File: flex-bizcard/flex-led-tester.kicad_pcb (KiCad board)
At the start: 2 copper layers, 71.8 x 34.6 mm, 4 parts

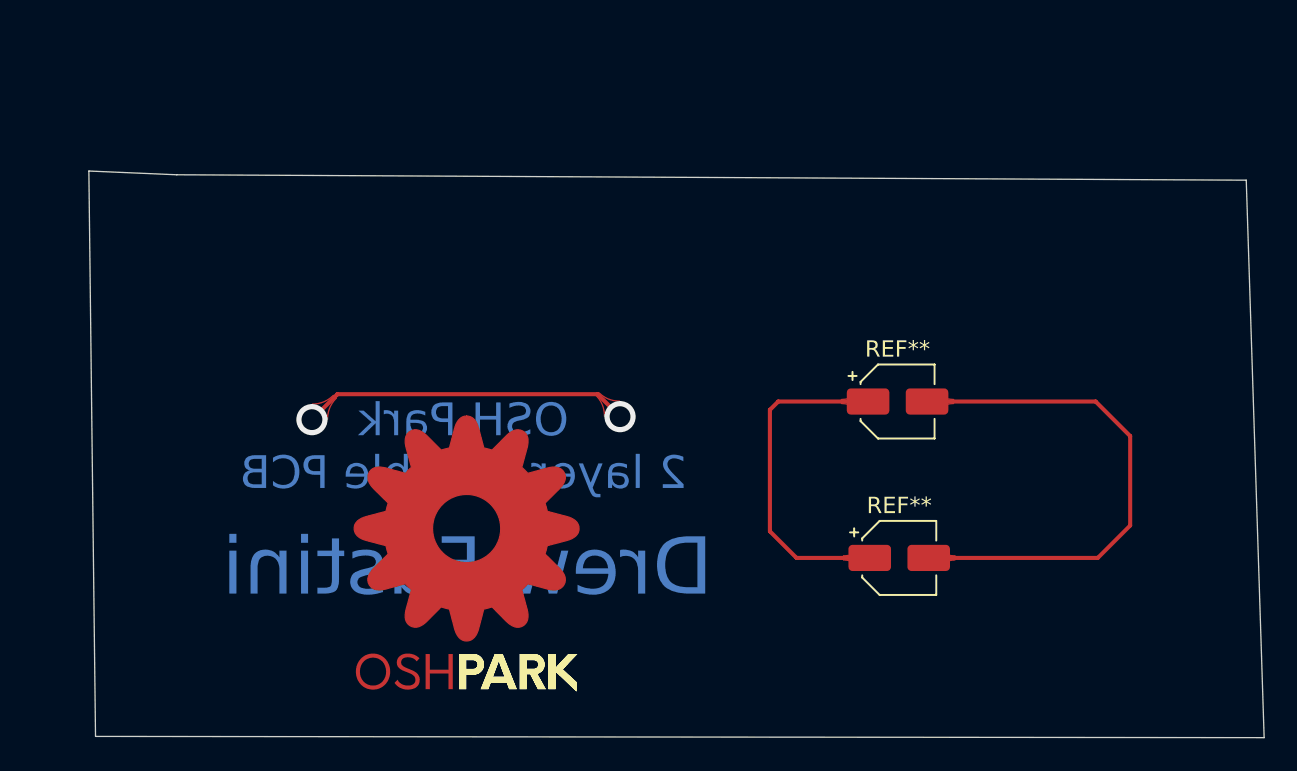
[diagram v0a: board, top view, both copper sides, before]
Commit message: create schematic and relayout flex batt tester
the teardrop plugin needs a schematic to work properly:
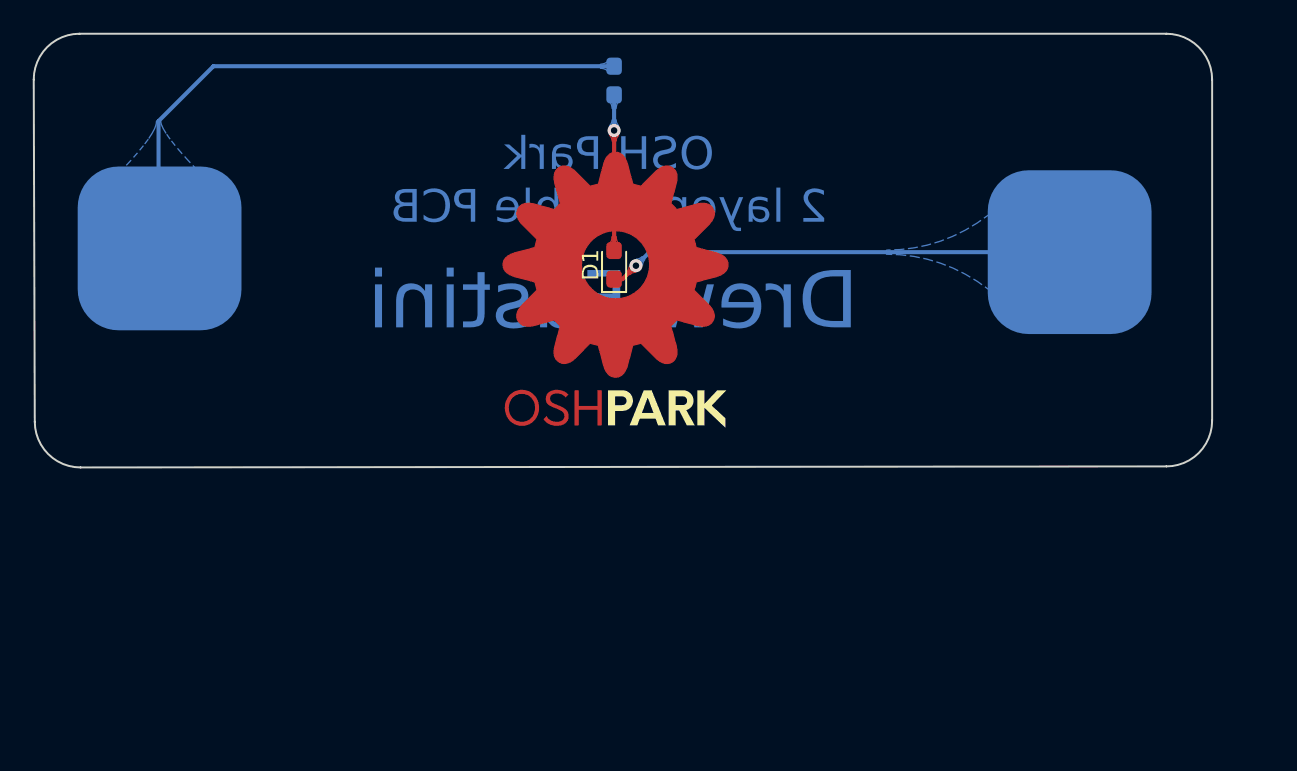
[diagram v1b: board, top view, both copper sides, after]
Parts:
- removed the OSH_small at (144.5, 72.4) (x2)
- removed REF** (x2): CP_Elec_4x3, Capacitor_SMD:CP_Elec_4x3
- added D1: LED, LED_SMD:LED_0603_1608Metric_Pad1.05x0.95mm_HandSolder, F.Cu at (153.5, 54.8)
- added J1: Conn_01x01_Female, touch:TestPoint_Pad_4.0x4.0mm, B.Cu at (125.7, 53.7)
- added J2: Conn_01x01_Female, touch:TestPoint_Pad_4.0x4.0mm, B.Cu at (181.3, 54.0)
- added OSH_small: G***, afterdark:OSH_small_copper-mask, F.Cu at (153.6, 56.3)
- added R1: R, Resistor_SMD:R_0603_1608Metric_Pad1.05x0.95mm_HandSolder, B.Cu at (153.5, 43.5)
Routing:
- net (no net): track 72.3 -> 0.00 mm, vias 2 -> 0
- net +3V3: track 0.00 -> 38.1 mm
- net GND: track 0.00 -> 29.1 mm, vias 0 -> 1
- net Net-(D1-Pad2): track 0.00 -> 9.48 mm, vias 0 -> 1
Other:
- board size 71.8 x 34.6 mm -> 71.9 x 26.5 mm
- board text added: "OSH Park 2 layer flexible PCB"
- board text removed: "OSH Park 2 layer Flexible PCB"

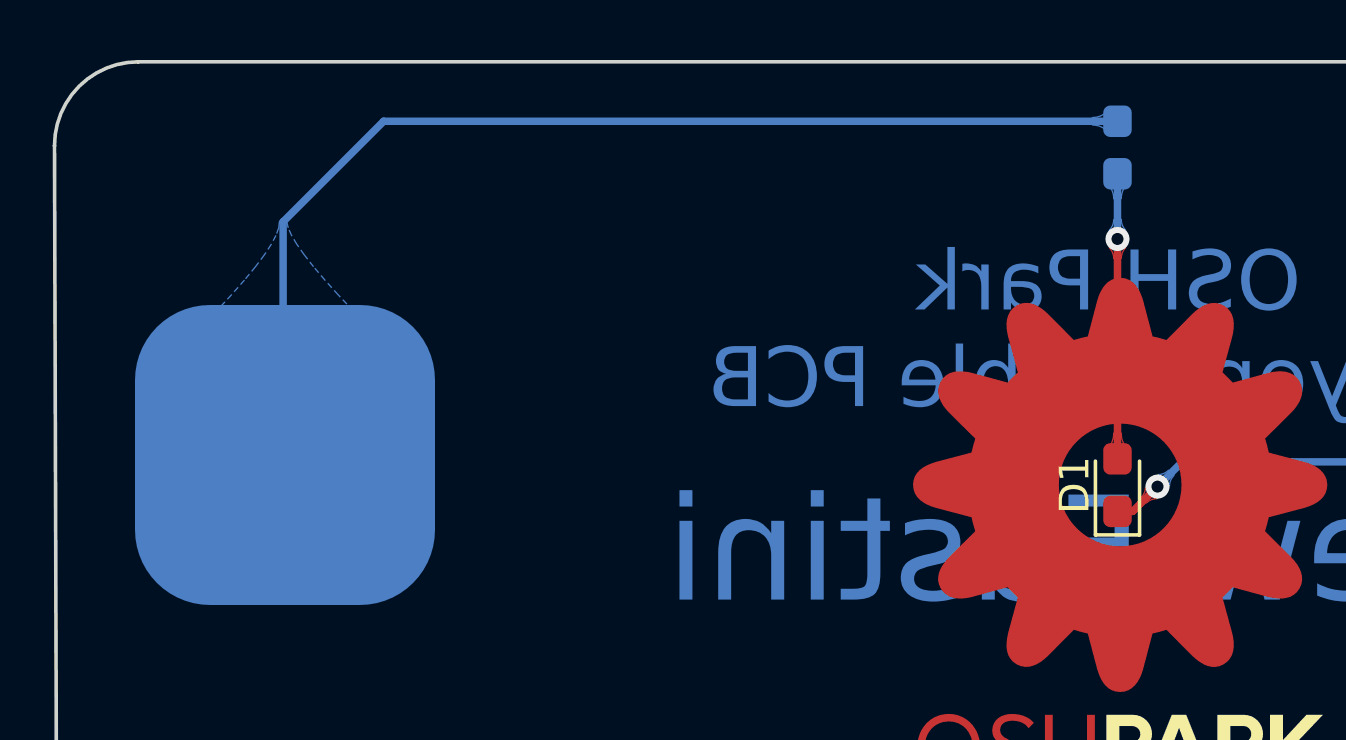
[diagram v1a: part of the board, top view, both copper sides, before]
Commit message: improve teardrops on the flex LED tester
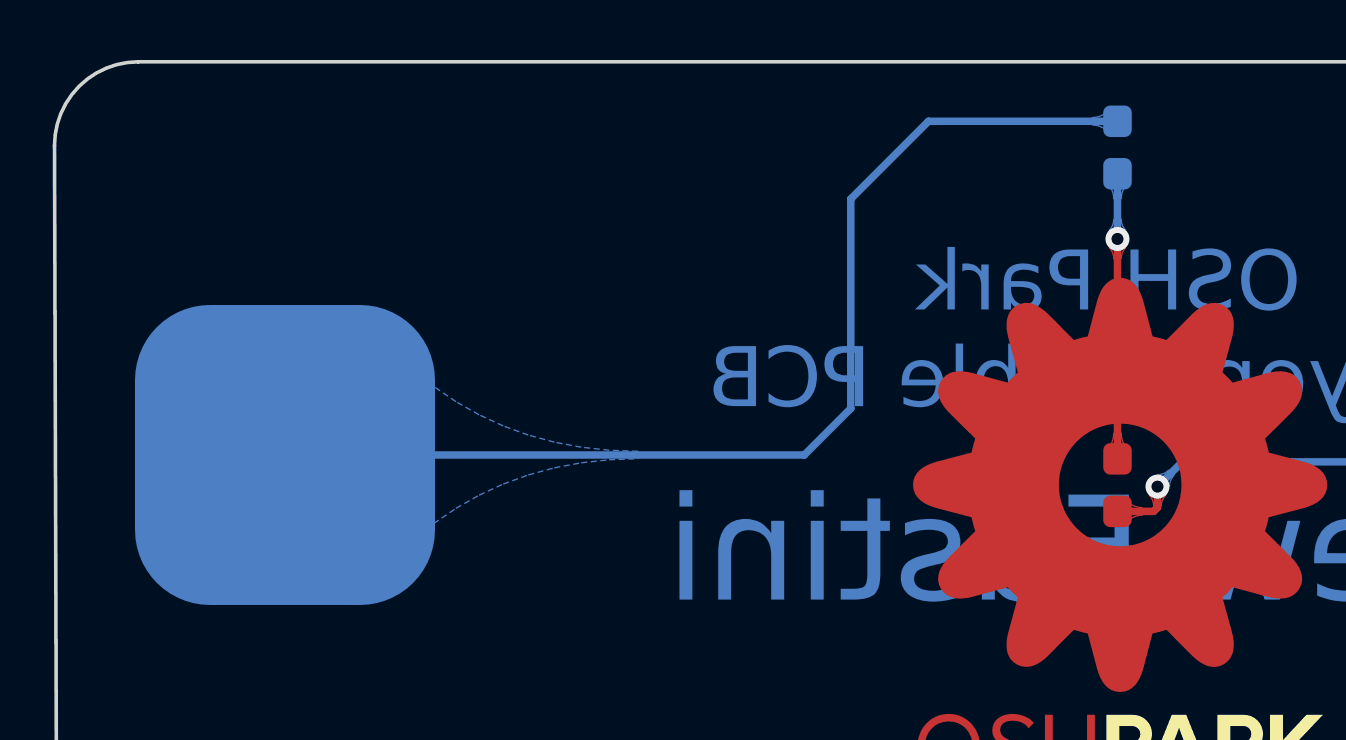
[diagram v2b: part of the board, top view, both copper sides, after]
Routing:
- net +3V3: track 38.1 -> 36.4 mm
